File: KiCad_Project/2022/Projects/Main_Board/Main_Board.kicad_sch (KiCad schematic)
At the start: 50 parts

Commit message: 回路図の完成
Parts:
- removed U?: Teensy4.0, herakuresu2022:Teensy, symbol Heracles.main-rescue:Teensy4.0-teensy
- removed U?: OpenMV, herakuresu2022:OpenMV, symbol Heracles.main-rescue:OpenMV-OpenMV
- removed U? (x2): SeeeduinoXIAO, herakuresu2022:seeeduinoXIAO, symbol Heracles.main-rescue:SeeeduinoXIAO-SeeeduinoXIAO
- added J?: Conn_01x04, symbol Connector_Generic:Conn_01x04
- added J?: (no value), symbol Connector_Generic:Conn_01x02
- added J?: (no value), symbol Connector_Generic:Conn_01x08
- added U?: SeeeduinoXIAO, symbol Seeeduino_XIAO:SeeeduinoXIAO
- added U?: (no value), symbol teensy:Teensy4.0
- added U?: (no value), symbol OpenMV:OpenMV
- added U?: (no value), symbol Seeeduino_XIAO:SeeeduinoXIAO
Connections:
- net +3V3: now also U?.31 (3V3)
- net +5V: now also J?.3 (Pin_3), J?.8 (Pin_8)
- net CS: now also U?.12 (10_CS_MQSR)
- net GND: now also J?.1 (Pin_1), J?.7 (Pin_7), U?.1 (GND), U?.1 (GND), U?.13 (GND), U?.13 (GND), U?.32 (GND), U?.47 (GND)
- net Intterapt: now also U?.29 (22_A8_CTX1)
- net Kicker: now also U?.8 (6_OUT1D)
- net MISO: now also U?.14 (12_MISO_MQSL)
- net MOSI: now also U?.13 (11_MOSI_CTX1)
- net RX1: now also J?.2 (Pin_2), U?.2 (0_RX1_CRX2_CS1)
- net RX2: now also U?.13 (P4), U?.9 (7_RX2_OUT1A)
- net RX3: now also U?.22 (15_A1_RX3_SPDIF_IN), U?.7 (PB08_A6_D6_TX)
- net RX4: now also U?.23 (16_A2_RX4_SCL1), U?.7 (PB08_A6_D6_TX)
- net RX5: now also U?.28 (21_A7_RX5_BCLK1)
- net RX6: now also J?.1 (Pin_1), U?.36 (25_A11_RX6_SDA2)
- net RX7: now also U?.39 (28_RX7)
- net SCK: now also U?.20 (13_SCK_CRX1_LED)
- net SW1: now also U?.38 (27_A13_SCK1)
- net SW2: now also U?.41 (30_CRX3)
- net SW3: now also U?.43 (32_OUT1B)
- net SW4: now also U?.42 (31_CTX3)
- net TX1: now also J?.4 (Pin_4), U?.3 (1_TX1_CTX2_MISO1)
- net TX2: now also U?.10 (8_TX2_IN1), U?.14 (P5)
- net TX3: now also U?.21 (14_A0_TX3_SPDIF_OUT), U?.8 (PB09_A7_D7_RX)
- net TX4: now also U?.24 (17_A3_TX4_SDA1), U?.8 (PB09_A7_D7_RX)
- net TX5: now also U?.27 (20_A6_TX5_LRCLK1)
- net TX6: now also J?.2 (Pin_2), U?.35 (24_A10_TX6_SCL2)
- net TX7: now also U?.40 (29_TX7)
- net at R?.1: now also U?.11 (9_OUT1C)
- net at J?.3 (Pin_3): now also U?.25 (18_A4_SDA0)
- net I2C: now reaches J?.2 (Pin_2)
- net I2C: now also U?.26 (19_A5_SCL0)
- net at J?.3 (Pin_3): now also U?.30 (23_A9_CRX1_MCLK1)
- net at C?.2, SW?.2 (B): now also U?.33 (VIN)
- net at D?.2 (A), J?.6 (Pin_6): now also U?.4 (2_OUT2)
- net at BZ?.1 (-): now also U?.44 (33_MCLK2)
- net at D?.2 (A), J?.5 (Pin_5): now also U?.5 (3_LRCLK2)
- net at J?.2 (D-): now also U?.53 (D-)
- net at J?.3 (D+): now also U?.54 (D+)
- net at D?.2 (A), J?.4 (Pin_4): now also U?.6 (4_BCLK2)
- net at D?.2 (A), J?.3 (Pin_3): now also U?.7 (5_IN2)
- net at SW?.2 (B): now also U?.2 (VIN)
- net at J?.3 (Pin_3): now also U?.1 (PA02_A0_D0)
- net at J?.2 (Pin_2): now also U?.10 (PA5_A9_D9_MISO)
- net at C?.1, SW?.1 (A): now also U?.14 (5V) (x2)
- net at J?.2 (Pin_2): now also U?.2 (PA4_A1_D1)
- net at J?.3 (Pin_3): now also U?.3 (PA10_A2_D2)
- net at J?.2 (Pin_2): now also U?.4 (PA11_A3_D3)
- net at J?.3 (Pin_3): now also U?.5 (PA8_A4_D4_SDA)
- net at J?.2 (Pin_2): now also U?.6 (PA9_A5_D5_SCL)
- net at J?.3 (Pin_3): now also U?.9 (PA7_A8_D8_SCK)
- net at SW?.2: now also U?.1 (PA02_A0_D0)
- net at U?.8 (INT): now also U?.2 (PA4_A1_D1)
- net at U?.4 (SDA): now also U?.5 (PA8_A4_D4_SDA)
- net at U?.3 (SCL): now also U?.6 (PA9_A5_D5_SCL)
- new net: J?.6 (Pin_6), U?.45 (34_DAT1_MISO2)
- new net: J?.5 (Pin_5), U?.46 (35_DAT0_MOSI2)
- new net: J?.4 (Pin_4), U?.48 (36_CLK_CS2)
- new net: J?.3 (Pin_3), U?.50 (37_CMD_SCK2)
- new net: J?.2 (Pin_2), U?.51 (38_DAT3_RX5)
- new net: J?.1 (Pin_1), U?.52 (39_DAT2_TX5)
- no-connect marks 42 -> 43
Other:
- note added: "3ch Time of Flight"
- note added: "ADNS9800"
- note added: "DSR1202"
- note added: "SPI"
- note removed: "UI switch"
- moved on the sheet: BZ?, C?, D?, J?, R?, SW?, U?

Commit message: ライブラリの参照問題？
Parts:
- J?: value (none) -> Conn_01x02
- J?: value (none) -> Conn_01x08
- U?: value (none) -> Teensy4.0
- U?: value (none) -> OpenMV
- U?: value (none) -> SeeeduinoXIAO
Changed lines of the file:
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@@
       (effects (font (size 1.27 1.27)) hide)
     )
-    (property "Value" "" (id 1) (at 69.85 70.9188 90)
+    (property "Value" "GND" (id 1) (at 69.85 70.9188 90)
       (effects (font (size 1.27 1.27)) (justify right))
     )
@@
     (in_bom yes) (on_board yes) (fields_autoplaced)
     (property "Reference" "J?" (id 0) (at 64.135 33.1302 0))
-    (property "Value" "" (id 1) (at 64.135 35.6671 0))
+    (property "Value" "Conn_01x02" (id 1) (at 64.135 35.6671 0))
     (property "Footprint" "" (id 2) (at 64.135 40.64 0)
       (effects (font (size 1.27 1.27)) hide)
@@
       (effects (font (size 1.27 1.27)) hide)
     )
-    (property "Value" "" (id 1) (at 75.5651 73.4588 90)
+    (property "Value" "GND" (id 1) (at 75.5651 73.4588 90)
       (effects (font (size 1.27 1.27)) (justify right))
     )
@@
   (symbol (lib_id "teensy:Teensy4.0") (at 106.68 56.515 180) (unit 1)
     (in_bom yes) (on_board yes) (fields_autoplaced)
-    (property "Reference" "U?" (id 0) (at 106.68 16.1122 0))
-    (property "Value" "" (id 1) (at 106.68 18.6491 0))
-    (property "Footprint" "" (id 2) (at 116.84 61.595 0)
-      (effects (font (size 1.27 1.27)) hide)
-    )
-    (property "Datasheet" "" (id 3) (at 116.84 61.595 0)
+    (property "Reference" "U?" (id 0) (at 106.68 96.9178 0))
+    (property "Value" "Teensy4.0" (id 1) (at 106.68 94.3809 0))
+    (property "Footprint" "" (id 2) (at 96.52 51.435 0)
+      (effects (font (size 1.27 1.27)) hide)
+    )
+    (property "Datasheet" "" (id 3) (at 96.52 51.435 0)
       (effects (font (size 1.27 1.27)) hide)
     )
@@
     (in_bom yes) (on_board yes) (fields_autoplaced)
     (property "Reference" "U?" (id 0) (at 227.965 112.6322 0))
-    (property "Value" "" (id 1) (at 227.965 115.1691 0))
+    (property "Value" "OpenMV" (id 1) (at 227.965 115.1691 0))
     (property "Footprint" "" (id 2) (at 227.965 113.665 0)
       (effects (font (size 1.27 1.27)) hide)
@@
     (in_bom yes) (on_board yes) (fields_autoplaced)
     (property "Reference" "J?" (id 0) (at 61.595 62.9752 0))
-    (property "Value" "" (id 1) (at 61.595 65.5121 0))
+    (property "Value" "Conn_01x08" (id 1) (at 61.595 65.5121 0))
     (property "Footprint" "" (id 2) (at 61.595 78.105 0)
       (effects (font (size 1.27 1.27)) hide)
@@
       (effects (font (size 1.27 1.27)) hide)
     )
-    (property "Value" "" (id 1) (at 69.85 68.3788 90)
+    (property "Value" "+5V" (id 1) (at 69.85 68.3788 90)
       (effects (font (size 1.27 1.27)) (justify left))
     )
@@
       (effects (font (size 1.27 1.27)) (justify left))
     )
-    (property "Value" "" (id 1) (at 74.4094 156.2053 0)
-      (effects (font (size 1.27 1.27)) (justify left))
-    )
+    (property "Value" "SeeeduinoXIAO" (id 1) (at 74.4094 156.2053 0)
+      (effects (font (size 1.27 1.27)) (justify left))
+    )

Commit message: マウス基板の改良
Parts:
- SW8, SW9: renamed from SW?; footprint herakuresu2022:PushSwitch -> (none)
- U1: renamed from U?; footprint herakuresu2022:MPU6050 -> (none)
- gave numbers to parts that had none: 50

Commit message: ライブラリの参照問題
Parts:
- removed U1: module_mpu6050, symbol Heracles.main-rescue:module_mpu6050-usini_sensors
- removed U2: Stamp_Pico, symbol StampPico_template:Stamp_Pico
- removed U3, U5: SeeeduinoXIAO, symbol Seeeduino_XIAO:SeeeduinoXIAO
- removed U4: Teensy4.0, symbol teensy:Teensy4.0
- removed U7: OpenMV, symbol OpenMV:OpenMV
- added U? (x2): (no value), symbol Seeeduino XIAO:SeeeduinoXIAO
- added U?: (no value), symbol OpenMV:OpenMV
- added U?: (no value), symbol StampPico_template:Stamp_Pico
- added U?: (no value), symbol teensy:Teensy4.0
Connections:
- net +3V3: now also U?.31 (3V3)
- net CS: now also U?.12 (10_CS_MQSR)
- net GND: now also U?.1 (GND), U?.1 (GND), U?.13 (GND), U?.13 (GND), U?.32 (GND), U?.47 (GND)
- net I2C: now also U?.26 (19_A5_SCL0)
- net Intterapt: now also U?.29 (22_A8_CTX1)
- net Kicker: now also U?.8 (6_OUT1D)
- net MISO: now also U?.14 (12_MISO_MQSL)
- net MOSI: now also U?.13 (11_MOSI_CTX1)
- net RX1: now also U?.2 (0_RX1_CRX2_CS1)
- net RX2: now also U?.13 (P4), U?.9 (7_RX2_OUT1A)
- net RX3: now also U?.22 (15_A1_RX3_SPDIF_IN), U?.7 (PB08_A6_D6_TX)
- net RX4: now also U?.23 (16_A2_RX4_SCL1), U?.7 (PB08_A6_D6_TX)
- net RX5: now also U?.28 (21_A7_RX5_BCLK1)
- net RX6: now also U?.36 (25_A11_RX6_SDA2)
- net RX7: now also U?.39 (28_RX7)
- net SCK: now also U?.20 (13_SCK_CRX1_LED)
- net SW1: now also U?.38 (27_A13_SCK1)
- net SW2: now also U?.41 (30_CRX3)
- net SW3: now also U?.43 (32_OUT1B)
- net SW4: now also U?.42 (31_CTX3)
- net TX1: now also U?.3 (1_TX1_CTX2_MISO1)
- net TX2: now also U?.10 (8_TX2_IN1), U?.14 (P5)
- net TX3: now also U?.21 (14_A0_TX3_SPDIF_OUT), U?.8 (PB09_A7_D7_RX)
- net TX4: now also U?.24 (17_A3_TX4_SDA1), U?.8 (PB09_A7_D7_RX)
- net TX5: now also U?.27 (20_A6_TX5_LRCLK1)
- net TX6: now also U?.35 (24_A10_TX6_SCL2)
- net TX7: now also U?.40 (29_TX7)
- net at SW1.2: now also U?.1 (PA02_A0_D0)
- net at J6.2 (Pin_2): now also U?.2 (PA4_A1_D1)
- net at J6.3 (Pin_3): now also U?.1 (PA02_A0_D0)
- net at J7.2 (Pin_2): now also U?.4 (PA11_A3_D3)
- net at J7.3 (Pin_3): now also U?.3 (PA10_A2_D2)
- net at J8.2 (Pin_2): now also U?.6 (PA9_A5_D5_SCL)
- net at J8.3 (Pin_3): now also U?.5 (PA8_A4_D4_SDA)
- net at J9.2 (Pin_2): now also U?.10 (PA5_A9_D9_MISO)
- net at J9.3 (Pin_3): now also U?.9 (PA7_A8_D8_SCK)
- net at D5.2 (A), J11.3 (Pin_3): now also U?.7 (5_IN2)
- net at D4.2 (A), J11.4 (Pin_4): now also U?.6 (4_BCLK2)
- net at D3.2 (A), J11.5 (Pin_5): now also U?.5 (3_LRCLK2)
- net at D2.2 (A), J11.6 (Pin_6): now also U?.4 (2_OUT2)
- net at BZ1.1 (-): now also U?.44 (33_MCLK2)
- net at C2.1, SW3.1 (A): now also U?.14 (5V)
- net at C3.1, SW4.1 (A): now also U?.14 (5V)
- net at C1.2, SW2.2 (B): now also U?.33 (VIN)
- net at J5.2 (D-): now also U?.53 (D-)
- net at J5.3 (D+): now also U?.54 (D+)
- net at SW5.2 (B): now also U?.2 (VIN)
- net at J2.3 (Pin_3): now also U?.30 (23_A9_CRX1_MCLK1)
- net at R2.1: now also U?.11 (9_OUT1C)
- net at J10.3 (Pin_3): now also U?.25 (18_A4_SDA0)
- net at J3.6 (Pin_6): now also U?.45 (34_DAT1_MISO2)
- net at J3.5 (Pin_5): now also U?.46 (35_DAT0_MOSI2)
- net at J3.4 (Pin_4): now also U?.48 (36_CLK_CS2)
- net at J3.3 (Pin_3): now also U?.50 (37_CMD_SCK2)
- net at J3.2 (Pin_2): now also U?.51 (38_DAT3_RX5)
- net at J3.1 (Pin_1): now also U?.52 (39_DAT2_TX5)

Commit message: 徹夜の進捗、朝マック食べに行きます
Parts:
- removed C4: CP, Capacitor_THT:C_Radial_D6.3mm_H11.0mm_P2.50mm, symbol Device:CP
- removed C5: C, Capacitor_THT:C_Disc_D3.0mm_W2.0mm_P2.50mm, symbol Device:C
- removed J14: Conn_01x04, symbol Connector_Generic:Conn_01x04
- removed J4: Conn_01x02, symbol Connector_Generic:Conn_01x02
- added C?: C_Small, Capacitor_THT:C_Disc_D3.0mm_W2.0mm_P2.50mm, symbol Device:C_Small
- added J?: Conn_01x03, symbol Connector_Generic:Conn_01x03
- added SW? (x2): SW_SPST, symbol Switch:SW_SPST
- added U?: module_mpu6050, usini_sensors:module_mpu6050, symbol usini_sensors:module_mpu6050
- SW6: footprint herakuresu2022:toggleswitch -> (none)
- U1: renamed from U?; value (none) -> Stamp_Pico
- U2, U4: renamed from U?; value (none) -> SeeeduinoXIAO
- U3: renamed from U?; value (none) -> Teensy4.0
- U5: renamed from U?; value (none) -> OpenMV
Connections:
- net +5V: now also J10.3 (Pin_3), SW?.1 (A), SW?.2 (B), U?.1 (VCC); no longer J13.3 (Pin_3)
- net GND: now also J10.4 (Pin_4), C?.2, J?.1 (Pin_1), U?.2 (GND)
- net I2C: now also J10.1 (Pin_1); no longer J10.2 (Pin_2)
- net RX1: no longer J13.2 (Pin_2)
- net RX7: now also J13.2 (Pin_2)
- net TX1: no longer J13.4 (Pin_4)
- net TX7: now also J13.3 (Pin_3)
- net at SW5.2 (B), U5.2 (VIN): now also C?.1
- net at U2.2 (PA4_A1_D1): now also U?.8 (INT)
- net at U2.5 (PA8_A4_D4_SDA): now also U?.4 (SDA)
- net at U2.6 (PA9_A5_D5_SCL): now also U?.3 (SCL)
- net at U3.25 (18_A4_SDA0): now also J10.2 (Pin_2); no longer J10.3 (Pin_3)
- net NeoPixel: now reaches U3.37 (26_A12_MOSI1)
- new net: J13.4 (Pin_4), SW?.1 (A)
- new net: J?.2 (Pin_2), SW?.2 (B)
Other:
- moved on the sheet: BZ1, C1, C2, C3, C6, C7, C8, C9, D1, D2, D3, D4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

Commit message: フットプリントライブラリの編集
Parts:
- added C10, C4, C5: C_Small, Capacitor_THT:C_Disc_D3.0mm_W2.0mm_P2.50mm, symbol Device:C_Small
- added J14: Conn_01x02, symbol Connector_Generic:Conn_01x02
- added J4: Conn_01x03, symbol Connector_Generic:Conn_01x03
- added U8: Akizuki_Logiv_Level_converter, symbol Logic_Level_Converter:Akizuki_Logiv_Level_converter
- gave numbers to parts that had none: 5
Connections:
- net +3V3: now also U8.9 (LV)
- net +5V: now also U1.8 (5V), C10.1, C4.2, J4.2 (Pin_2), U8.4 (HV)
- net GND: now also U1.14 (GND), U1.9 (GND), C10.2, C4.1, C5.1, J4.1 (Pin_1), U8.10 (GND), U8.3 (GND)
- net NeoPixel: now also U8.7 (LV4)
- net RX5: now also U1.18 (G1)
- net RX6: now also U8.8 (LV3)
- net TX1: now also U8.12 (LV1)
- net TX5: now also U1.17 (G3)
- net TX6: now also U8.11 (LV2)
- net at J15.2 (Pin_2), SW11.2 (B): now also C5.2
- net at J15.3 (Pin_3): now also U8.1 (HV1)
- new net: J4.3 (Pin_3), U8.6 (HV4)
- new net: J14.1 (Pin_1), U8.2 (HV2)
- new net: J14.2 (Pin_2), U8.5 (HV3)
- no-connect marks 43 -> 57
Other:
- note added: "Mouse_Module"
- note added: "Neo_Pixel_Ring"
- moved on the sheet: U7

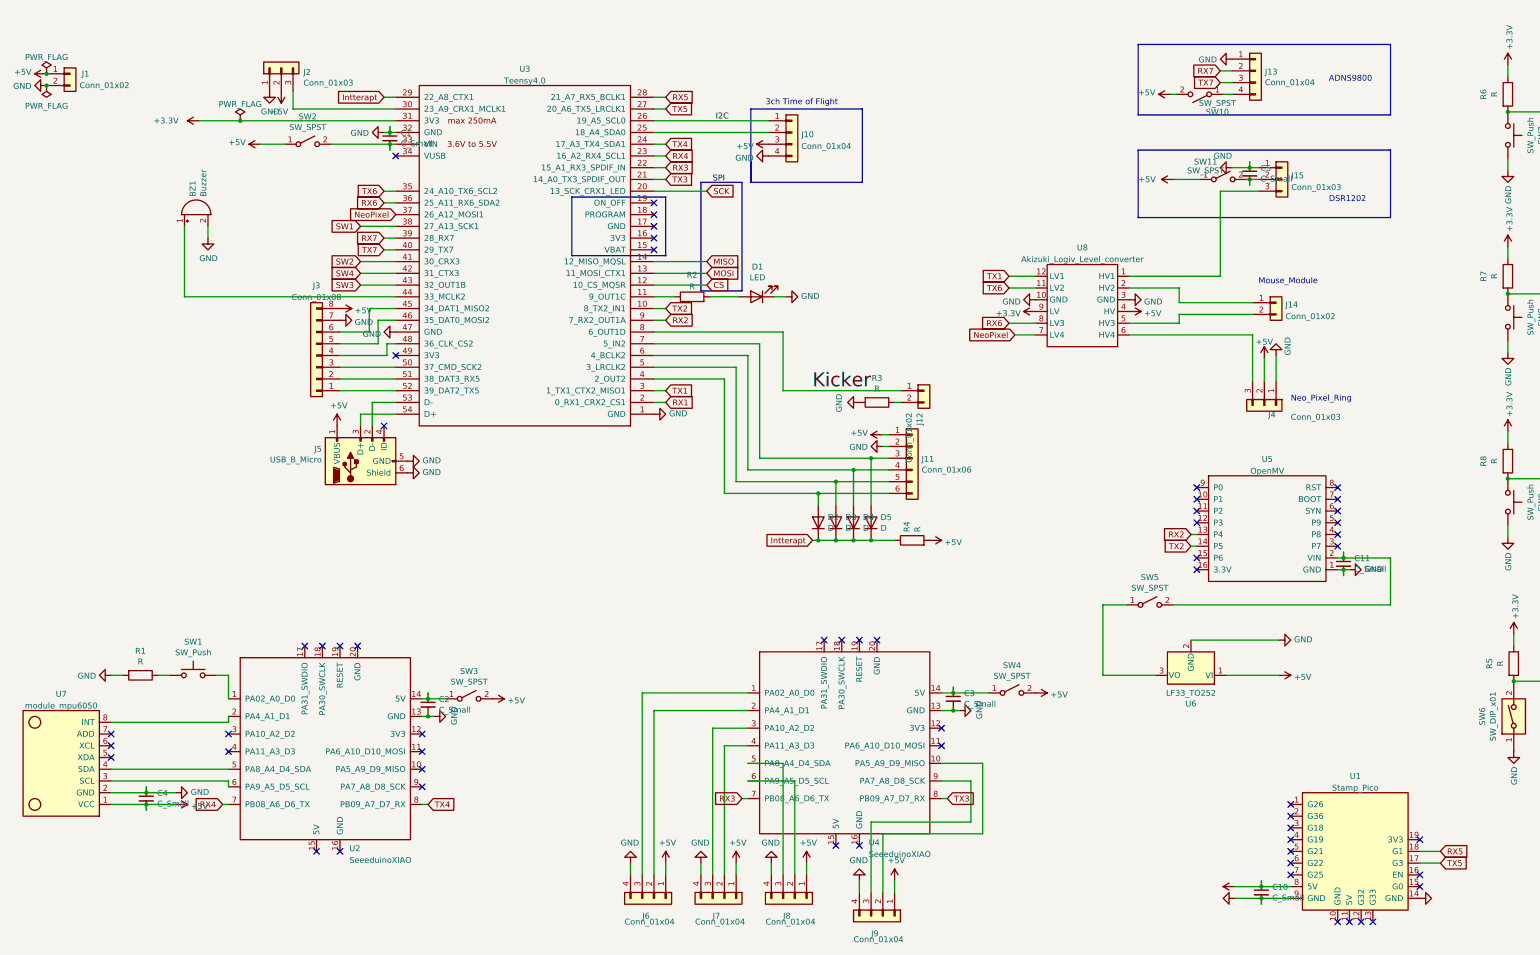
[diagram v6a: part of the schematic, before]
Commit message: フットプリントの割り当てまで終わった
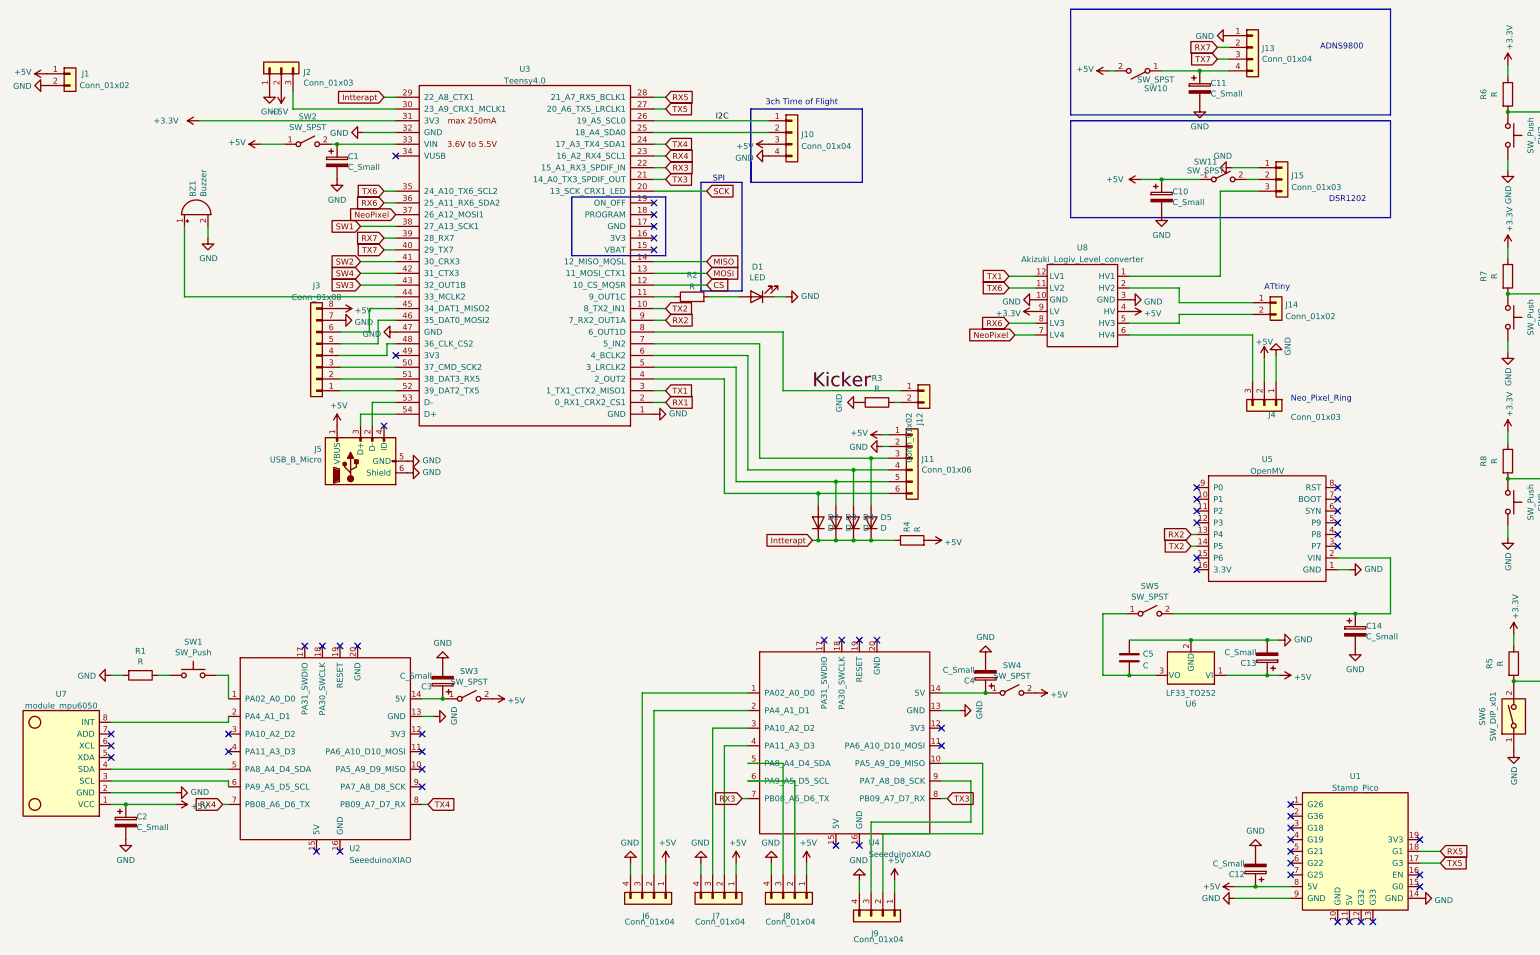
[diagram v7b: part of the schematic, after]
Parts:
- removed C10, C11, C2, C3, C4, C5: C_Small, Capacitor_THT:C_Disc_D3.0mm_W2.0mm_P2.50mm, symbol Device:C_Small
- added C10, C11, C12, C13, C14, C2, C3, C4: C_Small, Capacitor_THT:C_Radial_D6.3mm_H11.0mm_P2.50mm, symbol Device:C_Polarized
- added C5: C, Capacitor_THT:C_Disc_D3.0mm_W2.0mm_P2.50mm, symbol Device:C
- C1: footprint Capacitor_THT:C_Disc_D3.0mm_W2.0mm_P2.50mm -> Capacitor_THT:C_Radial_D6.3mm_H11.0mm_P2.50mm; symbol Device:C_Small -> Device:C_Polarized
- J10, J13: footprint (none) -> Connector_JST:JST_XH_B4B-XH-A_1x04_P2.50mm_Vertical
- J14: footprint (none) -> Connector_JST:JST_XH_B2B-XH-A_1x02_P2.50mm_Vertical
- J15, J2, J4: footprint (none) -> Connector_JST:JST_XH_B3B-XH-A_1x03_P2.50mm_Vertical
- J3: footprint (none) -> Connector_PinHeader_2.54mm:PinHeader_2x04_P2.54mm_Vertical
- J5: footprint (none) -> Library:MUSB5BF01AS
- R2: footprint (none) -> Resistor_THT:R_Axial_DIN0204_L3.6mm_D1.6mm_P5.08mm_Horizontal
- SW10, SW11, SW2, SW3, SW4, SW5, SW6: footprint (none) -> Library:toggleswitch
- SW8, SW9: footprint (none) -> Button_Switch_THT:SW_PUSH_6mm_H5mm
- U1: footprint (none) -> Library:StampPico_template
- U2, U4: footprint (none) -> Library:seeeduinoXIAO
- U3: footprint (none) -> Library:Teensy
- U5: footprint (none) -> Library:OpenMV
- U6: footprint Package_TO_SOT_SMD:TO-252-2 -> Connector_PinSocket_2.54mm:PinSocket_1x03_P2.54mm_Horizontal
- U8: footprint (none) -> Library:Akizuki_Logic_Level_converter
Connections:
- net +5V: now also C10.1, C12.1, C13.1, C2.1
- net GND: now also C1.2, C10.2, C11.2, C12.2, C13.2, C14.2, C2.2, C3.2, C4.2, C5.1; no longer C1.1
- net at SW5.1 (A), U6.3 (VO): now also C5.2
- net at SW3.1 (A), U2.14 (5V): now also C3.1
- net at SW4.1 (A), U4.14 (5V): now also C4.1
- net at SW2.2 (B), U3.33 (VIN): now also C1.1; no longer C1.2
- net at SW5.2 (B), U5.2 (VIN): now also C14.1
- net at J13.4 (Pin_4), SW10.1 (A): now also C11.1
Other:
- note added: "ATtiny"
- note removed: "Mouse_Module"
- moved on the sheet: J13, SW10, SW5
